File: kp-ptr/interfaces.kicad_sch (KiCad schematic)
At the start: 22 parts, among them IC1 E22-900M22S, J4 USB_C_Receptacle_USB2.0, J5 Micro_SD_Card_Det, U10 USBLC6-2SC6

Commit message: Weryfikacja footprintow faza I Signed-off-by: kretu <krecik@gmail.com>
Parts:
- added U?: W25Q128JVS, KP-PTR_lib:SON127P500X600X80-9N, symbol Memory_Flash:W25Q128JVS
- U?: value NC7WV04P6X -> NL27WZU04DBVT1G; footprint (none) -> KP-PTR_lib:SOT95P275X110-6N; symbol KP-PTR_lib:NC7WV04P6X -> KP-PTR_lib:NL27WZU04DBVT1G
- gave numbers to parts that had none: 10

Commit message: Footprinty drobnicy
Signed-off-by: kretu <krecik@gmail.com>
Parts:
- C37: footprint Capacitor_SMD:C_01005_0402Metric_Pad0.57x0.30mm_HandSolder -> Capacitor_SMD:C_0402_1005Metric_Pad0.74x0.62mm_HandSolder
- gave numbers to parts that had none: 2
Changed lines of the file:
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@@
   (symbol (lib_id "KP-PTR_lib:NL27WZU04DBVT1G") (at 196.85 66.04 0) (mirror y) (unit 1)
     (in_bom yes) (on_board yes)
-    (property "Reference" "U?" (id 0) (at 200.66 59.69 0))
+    (property "Reference" "U2" (id 0) (at 200.66 59.69 0))
     (property "Value" "NL27WZU04DBVT1G" (id 1) (at 196.85 69.85 0))
     (property "Footprint" "KP-PTR_lib:SOT95P275X110-6N" (id 2) (at 196.85 66.04 0))
@@
   (symbol (lib_id "Memory_Flash:W25Q128JVS") (at 217.17 124.46 0) (unit 1)
     (in_bom yes) (on_board yes) (fields_autoplaced)
-    (property "Reference" "U?" (id 0) (at 219.1894 111.76 0)
+    (property "Reference" "U11" (id 0) (at 219.1894 111.76 0)
       (effects (font (size 1.27 1.27)) (justify left))
     )
@@
       (effects (font (size 1.27 1.27)) (justify left))
     )
-    (property "Footprint" "Capacitor_SMD:C_01005_0402Metric_Pad0.57x0.30mm_HandSolder" (id 2) (at 101.2952 123.19 0)
-      (effects (font (size 1.27 1.27)) hide)
-    )
+    (property "Footprint" "Capacitor_SMD:C_0402_1005Metric_Pad0.74x0.62mm_HandSolder" (id 2) (at 101.2952 123.19 0)
+      (effects (font (size 1.27 1.27)) hide)
+    )

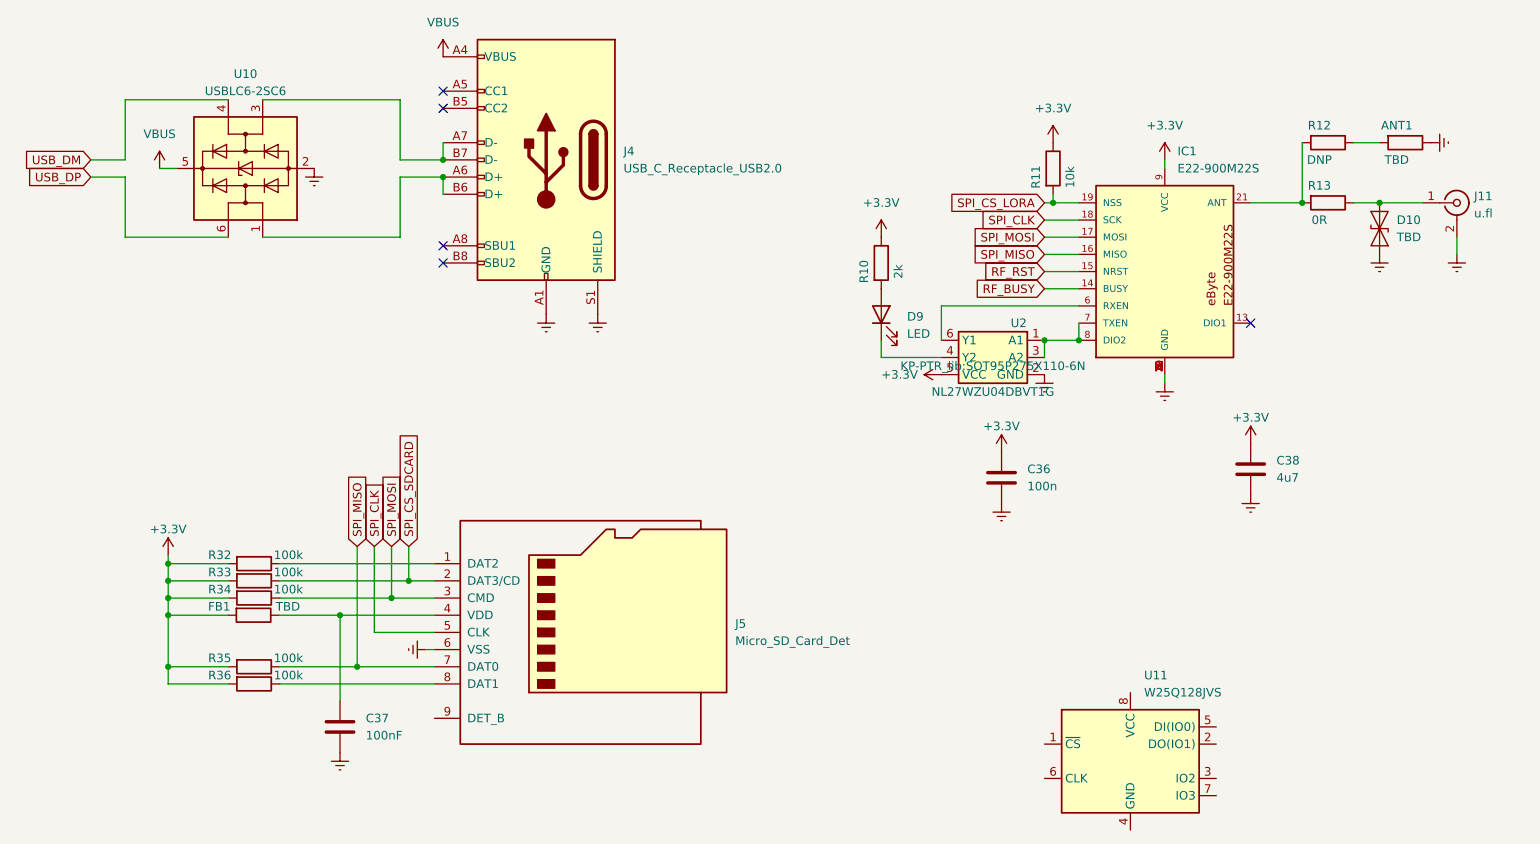
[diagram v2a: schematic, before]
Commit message: Removed SD card
Added Flash
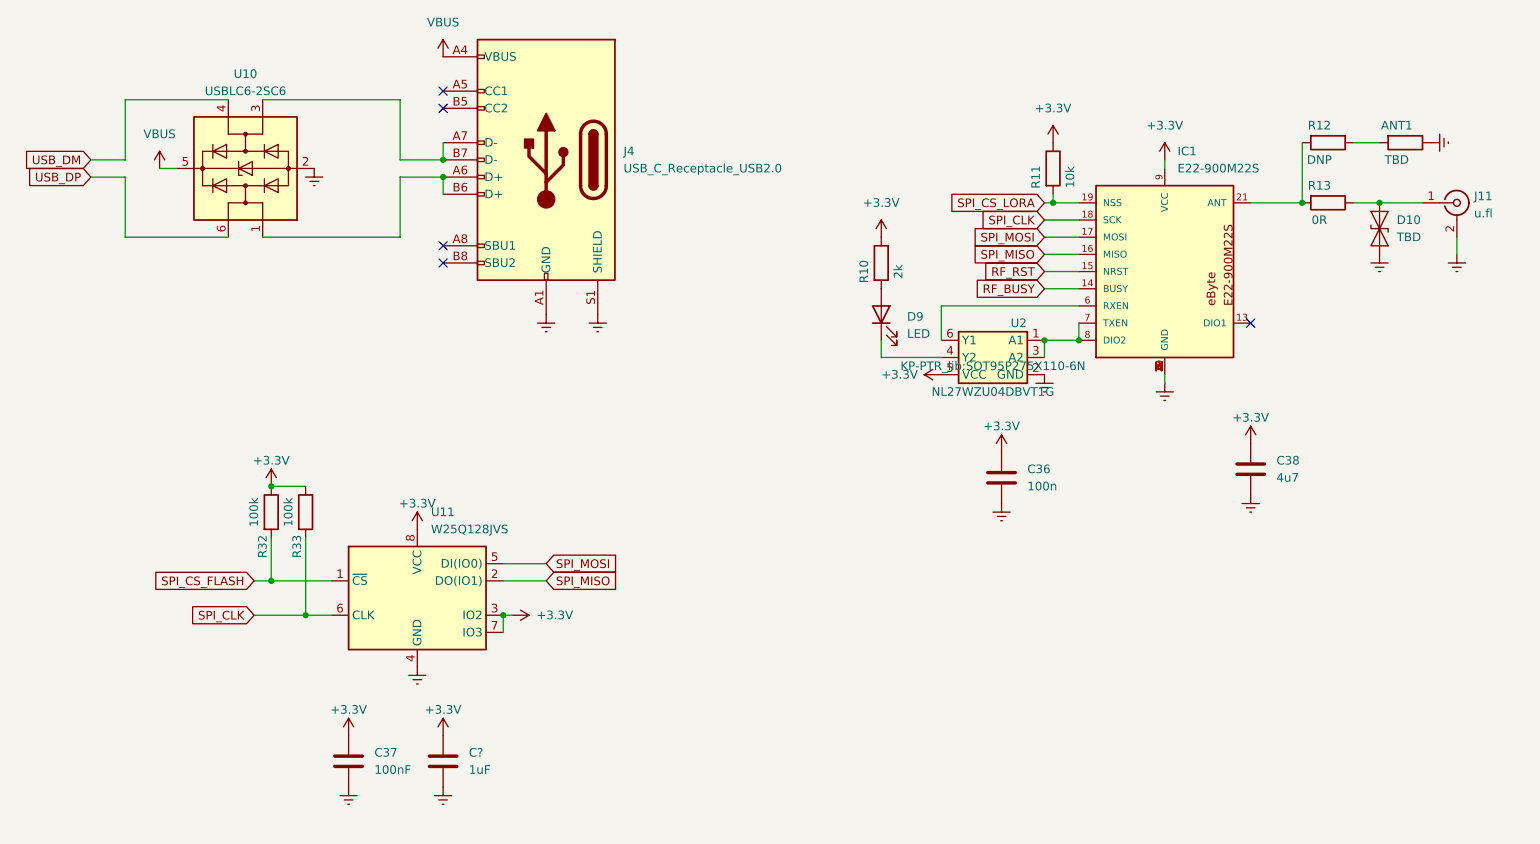
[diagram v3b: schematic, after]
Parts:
- removed FB1: TBD, Resistor_SMD:R_0402_1005Metric_Pad0.72x0.64mm_HandSolder, symbol Device:R
- removed J5: Micro_SD_Card_Det, KP-PTR_lib:GCT_MEM2051-00-195-00-A, symbol Connector:Micro_SD_Card_Det
- removed R34, R35, R36: 100k, Resistor_SMD:R_0402_1005Metric_Pad0.72x0.64mm_HandSolder, symbol Device:R
- added C?: 1uF, Capacitor_SMD:C_0402_1005Metric_Pad0.74x0.62mm_HandSolder, symbol Device:C
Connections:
- net SPI_CS_SDCARD is gone; now on net +3V3: R33.1
- net +3V3: now also C37.1, R32.1, U11.3 (IO2), U11.7 (IO3), U11.8 (VCC), C?.1; no longer R32.2, R33.2
- net Earth: now also U11.4 (GND), C?.2
- net SPI_CLK: now also R33.2, U11.6 (CLK)
- net SPI_MISO: now also U11.2 (DO(IO1))
- net SPI_MOSI: now also U11.5 (DI(IO0))
- net SPI_CS_FLASH: now reaches U11.1 (~{CS})
- net SPI_CS_FLASH: now also R32.2
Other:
- moved on the sheet: C37, R32, R33, U11

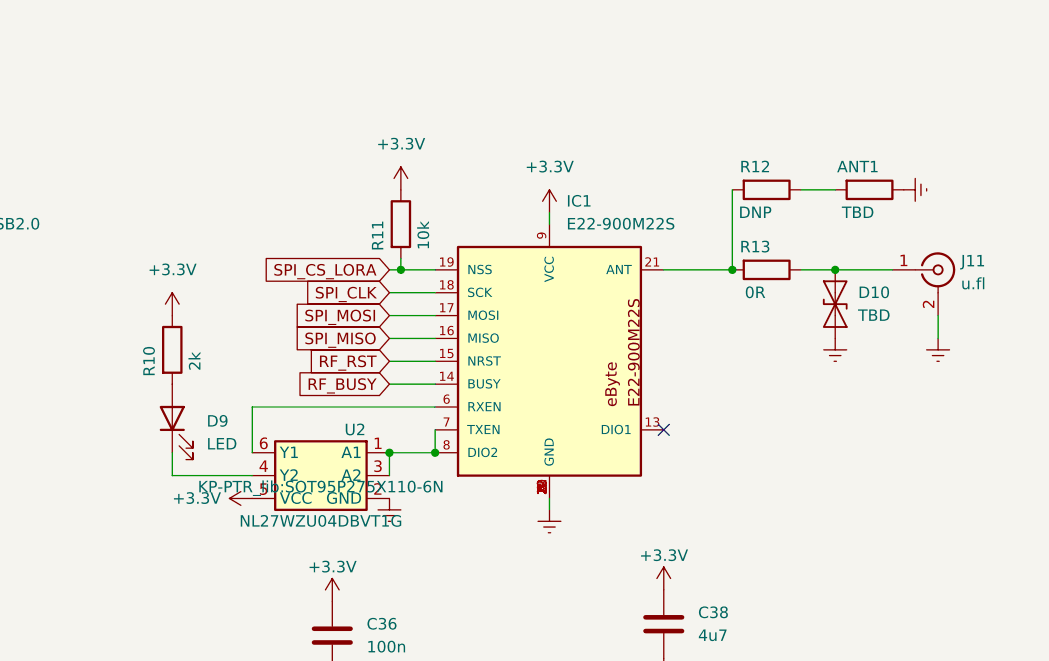
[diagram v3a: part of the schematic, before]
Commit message: Kilka zmian.
-dodany tranzystor P/N mosfet do biblioteki i zapalników
-dodany komentarz o impedancji ścieżek RF
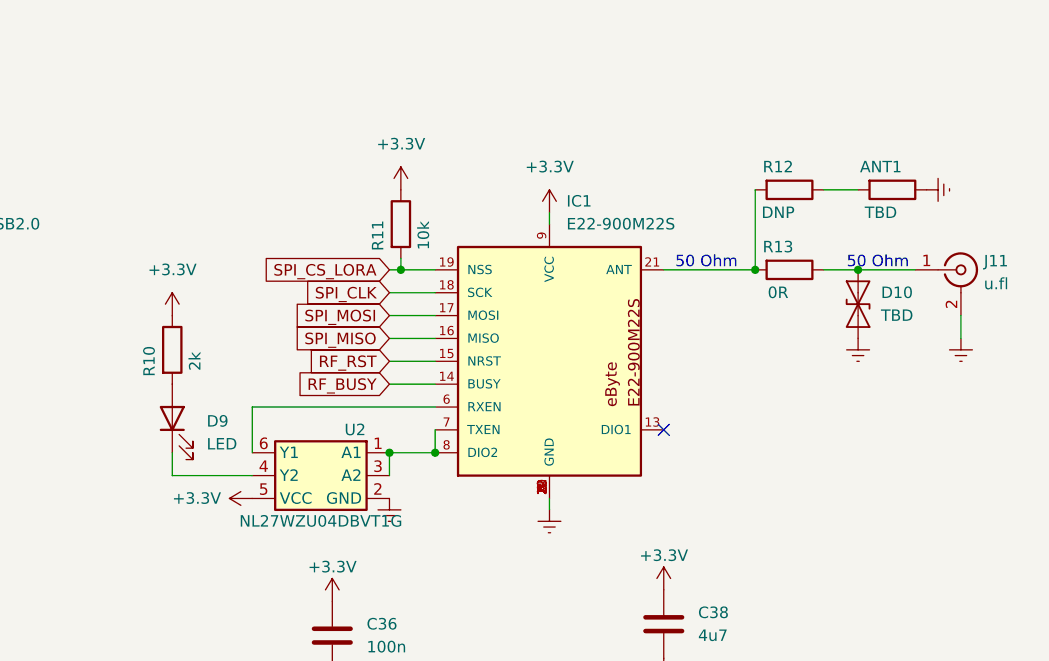
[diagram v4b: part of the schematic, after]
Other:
- note added: "50 Ohm"
- moved on the sheet: ANT1, D10, J11, R12, R13

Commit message: Szlifowanie schematu
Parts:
- added R?: 10k, Resistor_SMD:R_0402_1005Metric_Pad0.72x0.64mm_HandSolder, symbol Device:R
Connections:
- net +3V3: now also R?.1
- net RF_RST: now also R?.2
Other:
- moved on the sheet: D9, R10, U2

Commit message: Update po spotkaniu
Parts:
- added C47: 100n, Capacitor_SMD:C_0402_1005Metric, symbol Device:C
- added FB2: 1000mA, Resistor_SMD:R_0603_1608Metric, symbol Device:FerriteBead
- added R31: DNP, Resistor_SMD:R_0402_1005Metric, symbol Device:R
- C36, C37: footprint Capacitor_SMD:C_0402_1005Metric_Pad0.74x0.62mm_HandSolder -> Capacitor_SMD:C_0402_1005Metric
- C38: footprint Capacitor_SMD:C_0805_2012Metric_Pad1.18x1.45mm_HandSolder -> Capacitor_SMD:C_0402_1005Metric
- C46: renamed from C?; footprint Capacitor_SMD:C_0402_1005Metric_Pad0.74x0.62mm_HandSolder -> Capacitor_SMD:C_0402_1005Metric
- D10: footprint (none) -> Diode_SMD:D_SOD-123
- D9: footprint LED_SMD:LED_0402_1005Metric_Pad0.77x0.64mm_HandSolder -> LED_SMD:LED_0603_1608Metric
- J11: footprint (none) -> Connector_Coaxial:U.FL_Hirose_U.FL-R-SMT-1_Vertical
- J4: footprint KP-PTR_lib:217B-BC02 -> Connector_USB:USB_C_Receptacle_GCT_USB4085
- R10: value 2k -> 2k2; footprint Resistor_SMD:R_0402_1005Metric_Pad0.72x0.64mm_HandSolder -> Resistor_SMD:R_0402_1005Metric
- R11, R12, R13, R32, R33: footprint Resistor_SMD:R_0402_1005Metric_Pad0.72x0.64mm_HandSolder -> Resistor_SMD:R_0402_1005Metric
- R28: renamed from R?; footprint Resistor_SMD:R_0402_1005Metric_Pad0.72x0.64mm_HandSolder -> Resistor_SMD:R_0402_1005Metric
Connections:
- net +3V3: now also FB2.1; no longer C36.1, C38.1, IC1.9 (VCC), R10.1, R11.1, R28.1, U2.5 (VCC)
- net Earth: now also C47.2, R31.2
- net RF_RST: now also R31.1
- new net +3.3VP: C36.1, C38.1, C47.1, FB2.2, IC1.9 (VCC), R10.1, R11.1, R28.1, U2.5 (VCC)
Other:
- moved on the sheet: C36, D9, R10, U2

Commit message: Grupowanie
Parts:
- renumbered ANT1 to ANT3, C37 to C39, C46 to C40, C36 to C41, C47 to C42, C38 to C43, D9 to D8, D10 to D9, J11 to J5, R32 to R26, R33 to R27, R10 to R28, R28 to R29, R31 to R30, R11 to R31, R12 to R32, R13 to R33, U11 to U10, U2 to U11, U10 to U9

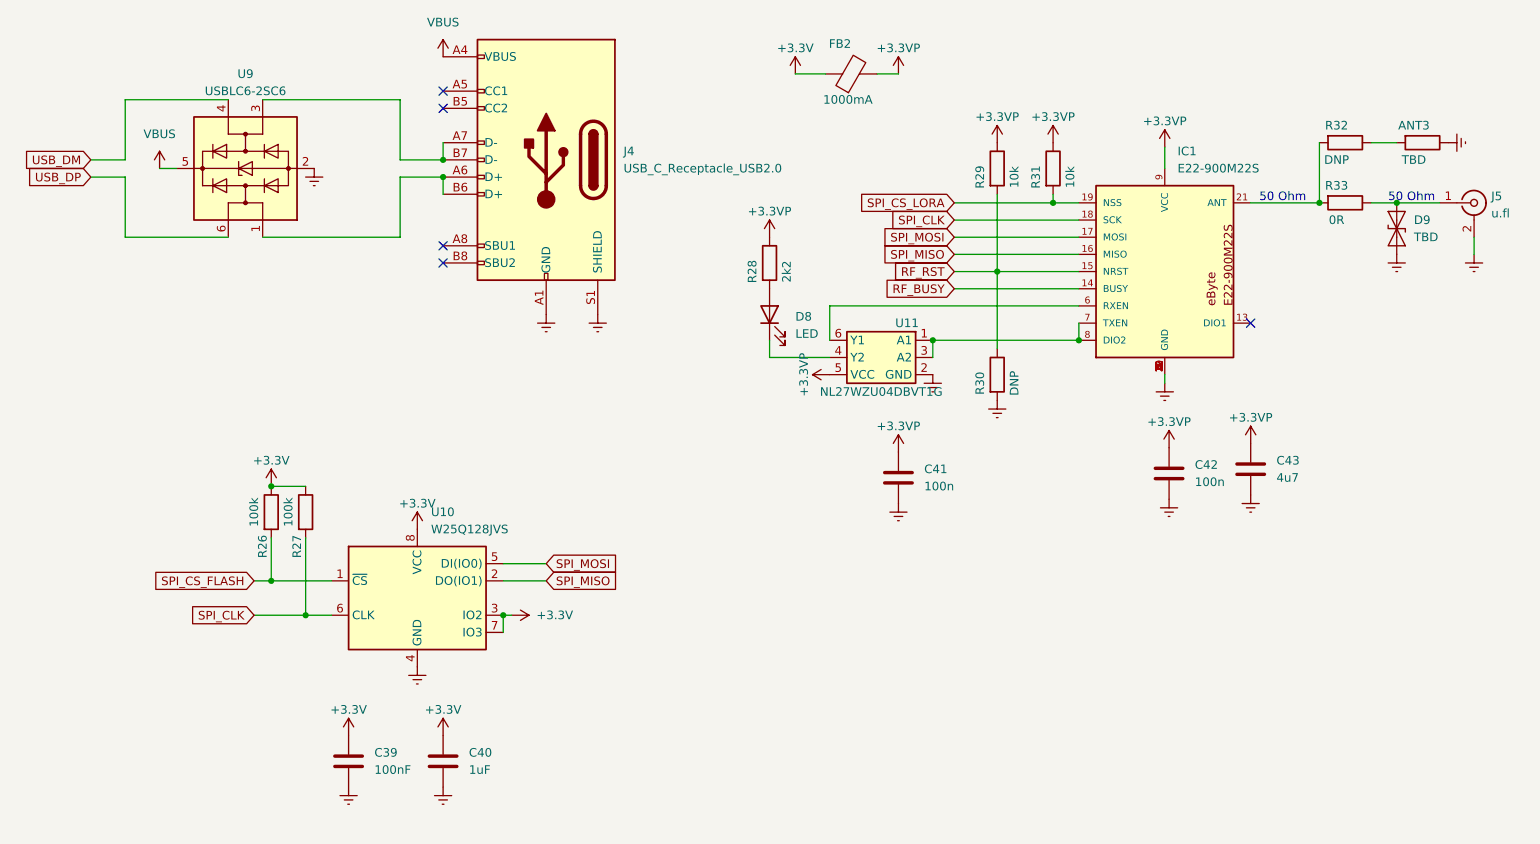
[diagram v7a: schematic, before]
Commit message: chyba wszystkie footprinty
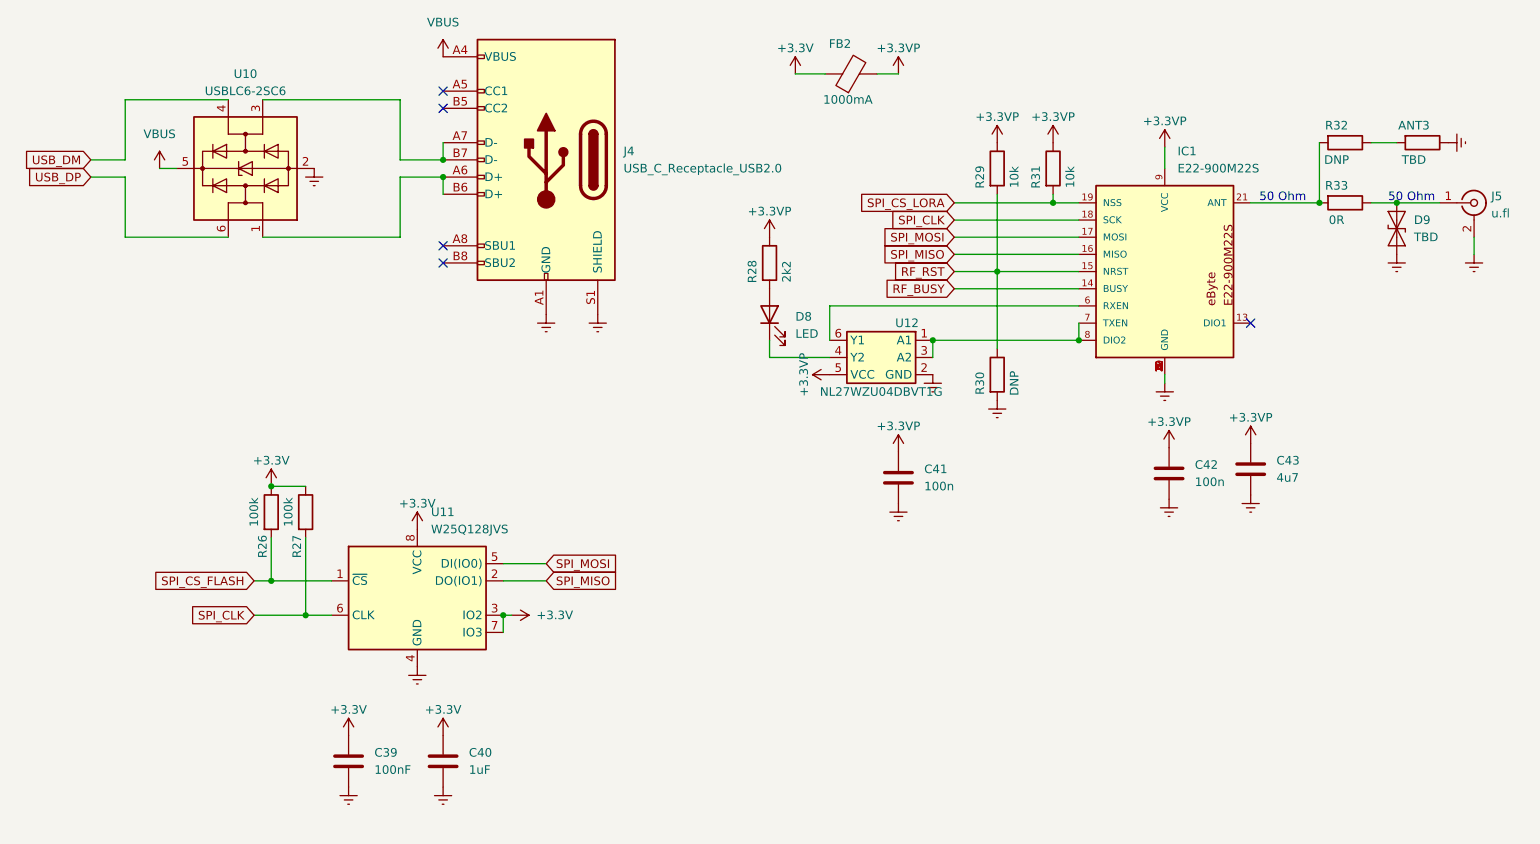
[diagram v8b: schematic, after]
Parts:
- renumbered U9 to U10, U10 to U11, U11 to U12
